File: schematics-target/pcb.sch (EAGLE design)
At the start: 8 parts, among them Q1 16Mhz

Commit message: Added target PCB board file
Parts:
- renumbered PROGRAMMER to TARGET_ATMEGA328P
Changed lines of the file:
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@@
 </classes>
 <parts>
-<part name="PROGRAMMER" library="atmega8" deviceset="ATMEGA48/88/168-PU" device=""/>
+<part name="TARGET_ATMEGA328P" library="atmega8" deviceset="ATMEGA48/88/168-PU" device=""/>
 <part name="R4" library="rcl" library_urn="urn:adsk.eagle:library:334" deviceset="R-EU_" device="R0805" package3d_urn="urn:adsk.eagle:package:23553/2" value="10k"/>
 <part name="P+4" library="supply1" library_urn="urn:adsk.eagle:library:371" deviceset="+5V" device=""/>
@@
 </plain>
 <instances>
-<instance part="PROGRAMMER" gate="1" x="76.2" y="48.26" smashed="yes">
+<instance part="TARGET_ATMEGA328P" gate="1" x="76.2" y="48.26" smashed="yes">
 <attribute name="NAME" x="50.8" y="81.28" size="1.778" layer="95" rot="MR180"/>
 <attribute name="VALUE" x="50.8" y="12.7" size="1.778" layer="96"/>
@@
 <wire x1="43.18" y1="27.94" x2="43.18" y2="25.4" width="0.1524" layer="91"/>
 <junction x="43.18" y="25.4"/>
-<pinref part="PROGRAMMER" gate="1" pin="GND@1"/>
-<pinref part="PROGRAMMER" gate="1" pin="AGND"/>
+<pinref part="TARGET_ATMEGA328P" gate="1" pin="GND@1"/>
+<pinref part="TARGET_ATMEGA328P" gate="1" pin="AGND"/>
 <pinref part="C10" gate="G$1" pin="1"/>
 <wire x1="33.02" y1="27.94" x2="33.02" y2="20.32" width="0.1524" layer="91"/>
@@
 <wire x1="43.18" y1="40.64" x2="43.18" y2="48.26" width="0.1524" layer="91"/>
 <junction x="43.18" y="48.26"/>
-<pinref part="PROGRAMMER" gate="1" pin="VCC@1"/>
-<pinref part="PROGRAMMER" gate="1" pin="AVCC"/>
+<pinref part="TARGET_ATMEGA328P" gate="1" pin="VCC@1"/>
+<pinref part="TARGET_ATMEGA328P" gate="1" pin="AVCC"/>
 <pinref part="C10" gate="G$1" pin="2"/>
 <wire x1="33.02" y1="48.26" x2="33.02" y2="35.56" width="0.1524" layer="91"/>
@@
 <segment>
 <pinref part="R4" gate="G$1" pin="2"/>
-<pinref part="PROGRAMMER" gate="1" pin="PC6(/RESET/PCINT14)"/>
+<pinref part="TARGET_ATMEGA328P" gate="1" pin="PC6(/RESET/PCINT14)"/>
 <wire x1="43.18" y1="76.2" x2="45.72" y2="76.2" width="0.1524" layer="91"/>
 <wire x1="45.72" y1="76.2" x2="45.72" y2="83.82" width="0.1524" layer="91"/>
@@
 <pinref part="Q1" gate="G$1" pin="2"/>
 <wire x1="35.56" y1="63.5" x2="45.72" y2="63.5" width="0.1524" layer="91"/>
-<pinref part="PROGRAMMER" gate="1" pin="PB6(XTAL1/TOSC1/PCINT6)"/>
+<pinref part="TARGET_ATMEGA328P" gate="1" pin="PB6(XTAL1/TOSC1/PCINT6)"/>
 <wire x1="45.72" y1="63.5" x2="45.72" y2="60.96" width="0.1524" layer="91"/>
 <pinref part="C1" gate="G$1" pin="2"/>
@@
 <net name="N$8" class="0">
 <segment>
-<pinref part="PROGRAMMER" gate="1" pin="PB7(XTAL2/TOSC2/PCINT7)"/>
+<pinref part="TARGET_ATMEGA328P" gate="1" pin="PB7(XTAL2/TOSC2/PCINT7)"/>
 <pinref part="Q1" gate="G$1" pin="1"/>
 <wire x1="45.72" y1="55.88" x2="45.72" y2="53.34" width="0.1524" layer="91"/>
@@
 <wire x1="45.72" y1="38.1" x2="43.18" y2="38.1" width="0.1524" layer="91"/>
 <wire x1="43.18" y1="38.1" x2="43.18" y2="35.56" width="0.1524" layer="91"/>
-<pinref part="PROGRAMMER" gate="1" pin="AREF"/>
+<pinref part="TARGET_ATMEGA328P" gate="1" pin="AREF"/>
 </segment>
 </net>
@@
 <segment>
 <pinref part="ISP" gate="G$1" pin="4"/>
-<pinref part="PROGRAMMER" gate="1" pin="PB3(MOSI/OC2A/PCINT3)"/>
+<pinref part="TARGET_ATMEGA328P" gate="1" pin="PB3(MOSI/OC2A/PCINT3)"/>
 <wire x1="119.38" y1="22.86" x2="106.68" y2="22.86" width="0.1524" layer="91"/>
 </segment>
@@
 <segment>
 <pinref part="ISP" gate="G$1" pin="1"/>
-<pinref part="PROGRAMMER" gate="1" pin="PB4(MISO/PCINT4)"/>
+<pinref part="TARGET_ATMEGA328P" gate="1" pin="PB4(MISO/PCINT4)"/>
 <wire x1="119.38" y1="20.32" x2="106.68" y2="20.32" width="0.1524" layer="91"/>
 </segment>
@@
 </segment>
 <segment>
-<pinref part="PROGRAMMER" gate="1" pin="PB5(SCK/PCINT5)"/>
+<pinref part="TARGET_ATMEGA328P" gate="1" pin="PB5(SCK/PCINT5)"/>
 <wire x1="106.68" y1="17.78" x2="109.22" y2="17.78" width="0.1524" layer="91"/>
 <wire x1="109.22" y1="17.78" x2="109.22" y2="15.24" width="0.1524" layer="91"/>

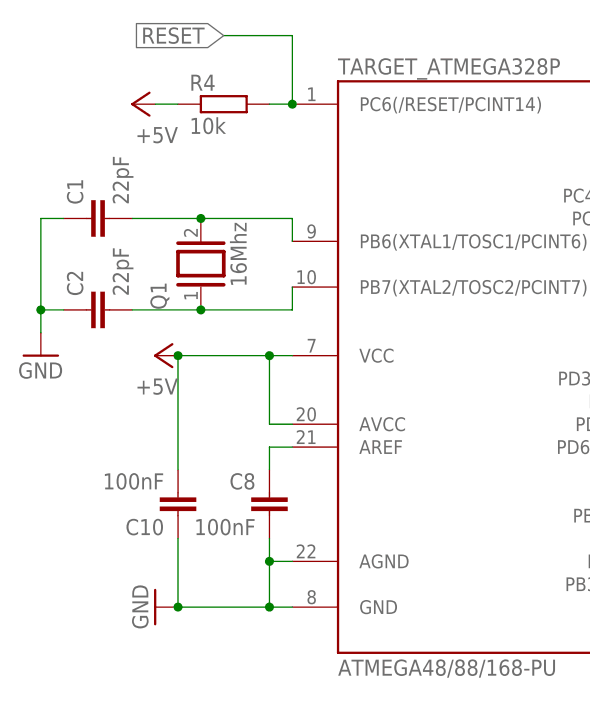
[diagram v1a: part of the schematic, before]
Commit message: Updated part names in target PCB
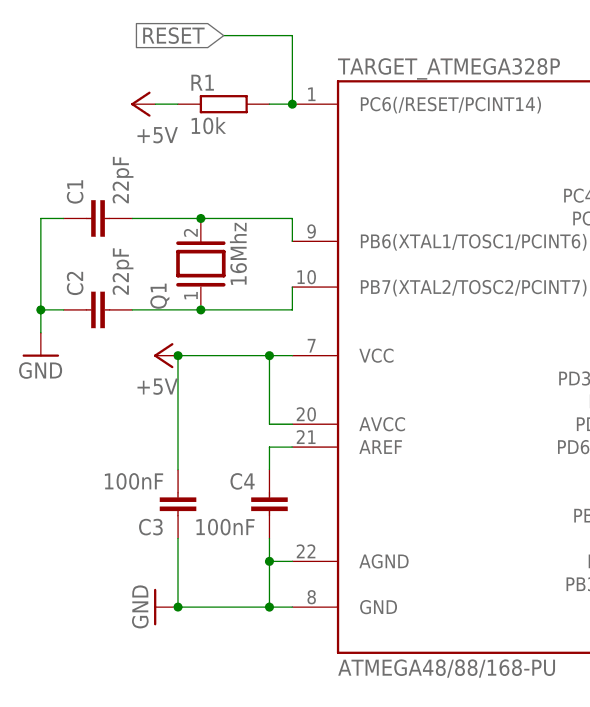
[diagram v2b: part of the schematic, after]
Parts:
- renumbered C10 to C3, C8 to C4, R4 to R1
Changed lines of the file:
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@@
 <parts>
 <part name="TARGET_ATMEGA328P" library="atmega8" deviceset="ATMEGA48/88/168-PU" device=""/>
-<part name="R4" library="rcl" library_urn="urn:adsk.eagle:library:334" deviceset="R-EU_" device="R0805" package3d_urn="urn:adsk.eagle:package:23553/2" value="10k"/>
+<part name="R1" library="rcl" library_urn="urn:adsk.eagle:library:334" deviceset="R-EU_" device="R0805" package3d_urn="urn:adsk.eagle:package:23553/2" value="10k"/>
 <part name="P+4" library="supply1" library_urn="urn:adsk.eagle:library:371" deviceset="+5V" device=""/>
 <part name="Q1" library="special" library_urn="urn:adsk.eagle:library:367" deviceset="XTAL/S" device="" package3d_urn="urn:adsk.eagle:package:26647/2" value="16Mhz"/>
@@
 <part name="P+10" library="supply1" library_urn="urn:adsk.eagle:library:371" deviceset="+5V" device=""/>
 <part name="GND16" library="supply1" library_urn="urn:adsk.eagle:library:371" deviceset="GND" device=""/>
-<part name="C8" library="rcl" library_urn="urn:adsk.eagle:library:334" deviceset="C-EU" device="C0805" package3d_urn="urn:adsk.eagle:package:23617/2" value="100nF"/>
-<part name="C10" library="rcl" library_urn="urn:adsk.eagle:library:334" deviceset="C-EU" device="C0805" package3d_urn="urn:adsk.eagle:package:23617/2" value="100nF"/>
+<part name="C4" library="rcl" library_urn="urn:adsk.eagle:library:334" deviceset="C-EU" device="C0805" package3d_urn="urn:adsk.eagle:package:23617/2" value="100nF"/>
+<part name="C3" library="rcl" library_urn="urn:adsk.eagle:library:334" deviceset="C-EU" device="C0805" package3d_urn="urn:adsk.eagle:package:23617/2" value="100nF"/>
 <part name="ISP" library="atmel" deviceset="AVR-ISP-6" device=""/>
 <part name="P+1" library="supply1" library_urn="urn:adsk.eagle:library:371" deviceset="+5V" device=""/>
@@
 <attribute name="VALUE" x="50.8" y="12.7" size="1.778" layer="96"/>
 </instance>
-<instance part="R4" gate="G$1" x="38.1" y="76.2" smashed="yes">
+<instance part="R1" gate="G$1" x="38.1" y="76.2" smashed="yes">
 <attribute name="NAME" x="34.29" y="77.6986" size="1.778" layer="95"/>
 <attribute name="VALUE" x="34.29" y="72.898" size="1.778" layer="96"/>
@@
 <attribute name="VALUE" x="27.94" y="22.86" size="1.778" layer="96" rot="R270"/>
 </instance>
-<instance part="C8" gate="G$1" x="43.18" y="33.02" smashed="yes" rot="MR0">
+<instance part="C4" gate="G$1" x="43.18" y="33.02" smashed="yes" rot="MR0">
 <attribute name="NAME" x="41.656" y="33.401" size="1.778" layer="95" rot="MR0"/>
 <attribute name="VALUE" x="41.656" y="28.321" size="1.778" layer="96" rot="MR0"/>
 </instance>
-<instance part="C10" gate="G$1" x="33.02" y="30.48" smashed="yes" rot="R180">
+<instance part="C3" gate="G$1" x="33.02" y="30.48" smashed="yes" rot="R180">
 <attribute name="NAME" x="31.496" y="30.099" size="1.778" layer="95" rot="R180"/>
 <attribute name="VALUE" x="31.496" y="35.179" size="1.778" layer="96" rot="R180"/>
@@
 <wire x1="43.18" y1="25.4" x2="43.18" y2="20.32" width="0.1524" layer="91"/>
 <junction x="43.18" y="20.32"/>
-<pinref part="C8" gate="G$1" pin="2"/>
+<pinref part="C4" gate="G$1" pin="2"/>
 <wire x1="43.18" y1="27.94" x2="43.18" y2="25.4" width="0.1524" layer="91"/>
 <junction x="43.18" y="25.4"/>
 <pinref part="TARGET_ATMEGA328P" gate="1" pin="GND@1"/>
 <pinref part="TARGET_ATMEGA328P" gate="1" pin="AGND"/>
-<pinref part="C10" gate="G$1" pin="1"/>
+<pinref part="C3" gate="G$1" pin="1"/>
 <wire x1="33.02" y1="27.94" x2="33.02" y2="20.32" width="0.1524" layer="91"/>
 <junction x="33.02" y="20.32"/>
@@
 <segment>
 <pinref part="P+4" gate="1" pin="+5V"/>
-<pinref part="R4" gate="G$1" pin="1"/>
+<pinref part="R1" gate="G$1" pin="1"/>
 <wire x1="30.48" y1="76.2" x2="33.02" y2="76.2" width="0.1524" layer="91"/>
 </segment>
@@
 <pinref part="TARGET_ATMEGA328P" gate="1" pin="VCC@1"/>
 <pinref part="TARGET_ATMEGA328P" gate="1" pin="AVCC"/>
-<pinref part="C10" gate="G$1" pin="2"/>
+<pinref part="C3" gate="G$1" pin="2"/>
 <wire x1="33.02" y1="48.26" x2="33.02" y2="35.56" width="0.1524" layer="91"/>
 <junction x="33.02" y="48.26"/>
@@
 <net name="RESET" class="0">
 <segment>
-<pinref part="R4" gate="G$1" pin="2"/>
+<pinref part="R1" gate="G$1" pin="2"/>
 <pinref part="TARGET_ATMEGA328P" gate="1" pin="PC6(/RESET/PCINT14)"/>
 <wire x1="43.18" y1="76.2" x2="45.72" y2="76.2" width="0.1524" layer="91"/>
@@
 <net name="N$22" class="0">
 <segment>
-<pinref part="C8" gate="G$1" pin="1"/>
+<pinref part="C4" gate="G$1" pin="1"/>
 <wire x1="45.72" y1="38.1" x2="43.18" y2="38.1" width="0.1524" layer="91"/>
 <wire x1="43.18" y1="38.1" x2="43.18" y2="35.56" width="0.1524" layer="91"/>
